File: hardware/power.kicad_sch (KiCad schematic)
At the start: 14 parts, among them U2 LM2596S-ADJ, U3 LM1117-5.0, U4 LM1117-3.3

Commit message: Assign footprints to symbols
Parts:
- C11, C12, C13, C14: footprint (none) -> Capacitor_SMD:C_0603_1608Metric
- D1: value 1N5822 -> SK36A-R2
- F1: footprint (none) -> Fuse:Fuse_1210_3225Metric
- L1: footprint (none) -> Inductor_SMD:L_12x12mm_H6mm
- R4, R5: footprint (none) -> Resistor_SMD:R_0603_1608Metric
- U3, U4: footprint (none) -> Package_TO_SOT_SMD:SOT-223-3_TabPin2
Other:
- moved on the sheet: C9
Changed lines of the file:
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@@
     (stroke (width 0) (type default) (color 0 0 0 0))
   )
-  (wire (pts (xy 85.09 95.25) (xy 85.09 100.33))
+  (wire (pts (xy 85.09 96.52) (xy 85.09 100.33))
     (stroke (width 0) (type default) (color 0 0 0 0))
   )
@@
     (stroke (width 0) (type default) (color 0 0 0 0))
   )
-  (wire (pts (xy 85.09 87.63) (xy 85.09 90.17))
+  (wire (pts (xy 85.09 87.63) (xy 85.09 91.44))
     (stroke (width 0) (type default) (color 0 0 0 0))
   )
@@
       (effects (font (size 1.27 1.27)) (justify left))
     )
-    (property "Footprint" "" (id 2) (at 227.33 97.79 0)
+    (property "Footprint" "Capacitor_SMD:C_0603_1608Metric" (id 2) (at 227.33 97.79 0)
       (effects (font (size 1.27 1.27)) hide)
     )
@@
       (effects (font (size 1.27 1.27)) (justify left))
     )
-    (property "Value" "1N5822" (id 1) (at 115.57 100.0124 90)
+    (property "Value" "SK36A-R2" (id 1) (at 113.03 100.0124 90)
       (effects (font (size 1.27 1.27)) (justify left))
     )
@@
     (property "Reference" "F1" (id 0) (at 76.2 82.55 90))
     (property "Value" "500mA" (id 1) (at 76.2 85.09 90))
-    (property "Footprint" "" (id 2) (at 81.28 86.36 0)
+    (property "Footprint" "Fuse:Fuse_1210_3225Metric" (id 2) (at 81.28 86.36 0)
       (effects (font (size 1.27 1.27)) (justify left) hide)
     )
@@
       (effects (font (size 1.27 1.27)) (justify right))
     )
-    (property "Footprint" "" (id 2) (at 207.01 97.79 0)
+    (property "Footprint" "Capacitor_SMD:C_0603_1608Metric" (id 2) (at 207.01 97.79 0)
       (effects (font (size 1.27 1.27)) hide)
     )
@@
     (property "Reference" "L1" (id 0) (at 130.81 90.17 90))
     (property "Value" "33μH" (id 1) (at 130.81 95.25 90))
-    (property "Footprint" "" (id 2) (at 130.81 92.71 0)
+    (property "Footprint" "Inductor_SMD:L_12x12mm_H6mm" (id 2) (at 130.81 92.71 0)
       (effects (font (size 1.27 1.27)) hide)
     )
@@
       (effects (font (size 1.27 1.27)) (justify left))
     )
-    (property "Footprint" "" (id 2) (at 190.5 97.79 0)
+    (property "Footprint" "Capacitor_SMD:C_0603_1608Metric" (id 2) (at 190.5 97.79 0)
       (effects (font (size 1.27 1.27)) hide)
     )
@@
     (property "Reference" "U4" (id 0) (at 217.17 86.36 0))
     (property "Value" "LM1117-3.3" (id 1) (at 217.17 88.9 0))
-    (property "Footprint" "" (id 2) (at 217.17 92.71 0)
+    (property "Footprint" "Package_TO_SOT_SMD:SOT-223-3_TabPin2" (id 2) (at 217.17 92.71 0)
       (effects (font (size 1.27 1.27)) hide)
     )
@@
     (property "Reference" "U3" (id 0) (at 180.34 86.36 0))
     (property "Value" "LM1117-5.0" (id 1) (at 180.34 88.9 0))
-    (property "Footprint" "" (id 2) (at 180.34 92.71 0)
+    (property "Footprint" "Package_TO_SOT_SMD:SOT-223-3_TabPin2" (id 2) (at 180.34 92.71 0)
       (effects (font (size 1.27 1.27)) hide)
     )
@@
       (effects (font (size 1.27 1.27)) (justify left))
     )
-    (property "Footprint" "" (id 2) (at 152.4 104.14 0)
+    (property "Footprint" "Resistor_SMD:R_0603_1608Metric" (id 2) (at 152.4 104.14 0)
       (effects (font (size 1.27 1.27)) hide)
     )
@@
     (pin "2")
   )
-  (symbol (lib_id "Device:C_Polarized_Small") (at 85.09 92.71 0) (unit 1)
-    (in_bom yes) (on_board yes) (fields_autoplaced)
-    (property "Reference" "C9" (id 0) (at 87.63 90.8938 0)
-      (effects (font (size 1.27 1.27)) (justify left))
-    )
-    (property "Value" "680μF" (id 1) (at 87.63 93.4338 0)
-      (effects (font (size 1.27 1.27)) (justify left))
-    )
-    (property "Footprint" "" (id 2) (at 85.09 92.71 0)
-      (effects (font (size 1.27 1.27)) hide)
-    )
-    (property "Datasheet" "~" (id 3) (at 85.09 92.71 0)
+  (symbol (lib_id "Device:C_Polarized_Small") (at 85.09 93.98 0) (unit 1)
+    (in_bom yes) (on_board yes) (fields_autoplaced)
+    (property "Reference" "C9" (id 0) (at 87.63 92.1638 0)
+      (effects (font (size 1.27 1.27)) (justify left))
+    )
+    (property "Value" "680μF" (id 1) (at 87.63 94.7038 0)
+      (effects (font (size 1.27 1.27)) (justify left))
+    )
+    (property "Footprint" "" (id 2) (at 85.09 93.98 0)
+      (effects (font (size 1.27 1.27)) hide)
+    )
+    (property "Datasheet" "~" (id 3) (at 85.09 93.98 0)
       (effects (font (size 1.27 1.27)) hide)
     )
@@
       (effects (font (size 1.27 1.27)) (justify right))
     )
-    (property "Footprint" "" (id 2) (at 170.18 97.79 0)
+    (property "Footprint" "Capacitor_SMD:C_0603_1608Metric" (id 2) (at 170.18 97.79 0)
       (effects (font (size 1.27 1.27)) hide)
     )
@@
       (effects (font (size 1.27 1.27)) (justify left))
     )
-    (property "Footprint" "" (id 2) (at 152.4 96.52 0)
-      (effects (font (size 1.27 1.27)) hide)
-    )
+    (property "Footprint" "Resistor_SMD:R_0603_1608Metric" (id 2) (at 152.4 96.52 0)
+      (effects (font (size 1.27 1.27)) hide)
+    )

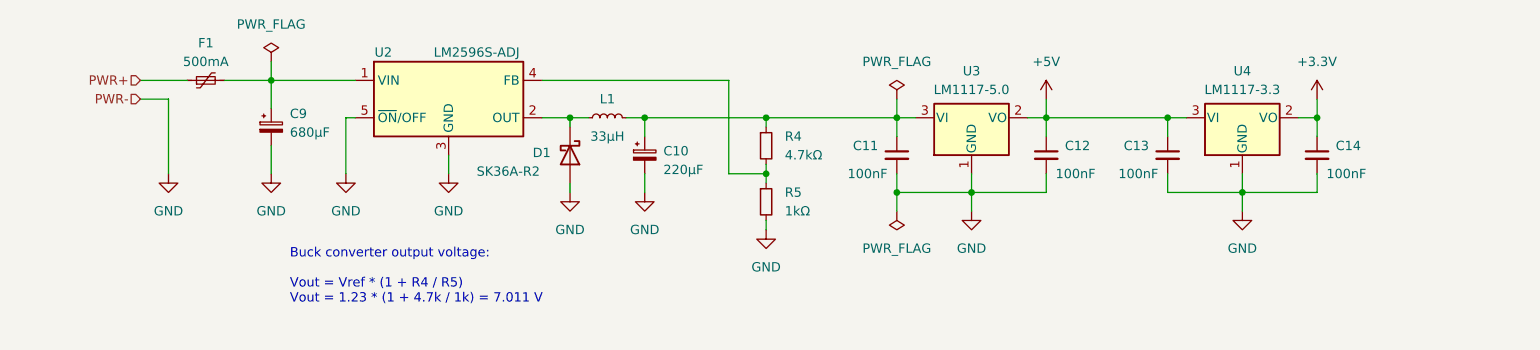
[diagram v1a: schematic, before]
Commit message: Use more efficient buck converter
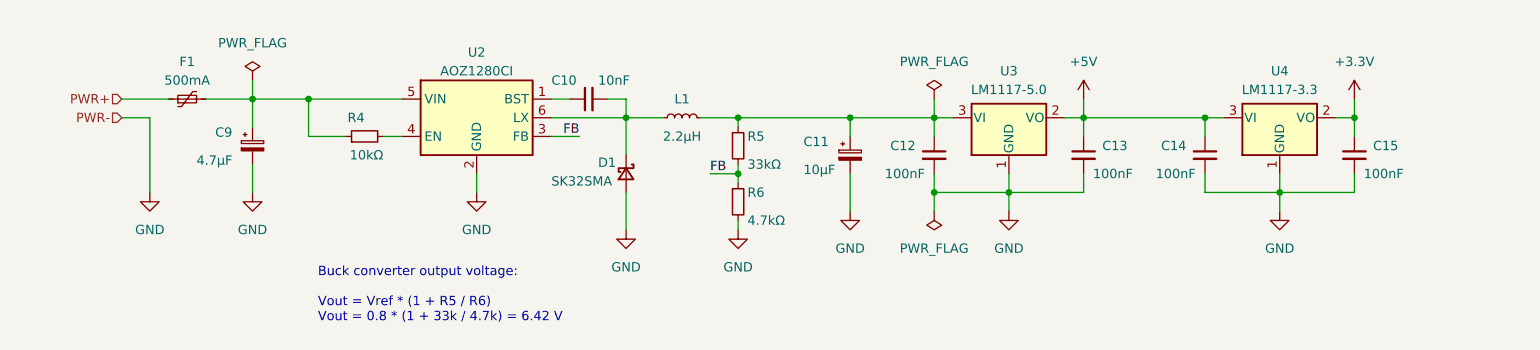
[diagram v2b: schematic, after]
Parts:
- removed D1: SK36A-R2, Diode_THT:D_DO-201AD_P15.24mm_Horizontal, symbol Diode:1N5822
- removed U2: LM2596S-ADJ, Package_TO_SOT_SMD:TO-263-5_TabPin3, symbol Regulator_Switching:LM2596S-ADJ
- added C10: 10nF, Capacitor_SMD:C_0603_1608Metric, symbol Device:C_Small
- added D1: SK32SMA, Diode_SMD:D_SMA, symbol Device:D_Schottky_Small
- added R4: 10kΩ, Resistor_SMD:R_0603_1608Metric, symbol Device:R_Small
- added U2: AOZ1280CI, Package_TO_SOT_SMD:SOT-23-6, symbol Regulator_Switching:AOZ1280CI
- C11: renamed from C10; value 220μF -> 10μF; footprint (none) -> Capacitor_SMD:C_Elec_4x5.4
- C9: value 680μF -> 4.7μF; footprint (none) -> Capacitor_SMD:C_Elec_4x5.4
- L1: value 33μH -> 2.2μH; footprint Inductor_SMD:L_12x12mm_H6mm -> Inductor_SMD:L_Bourns-SRN4018
- R5: renamed from R4; value 4.7kΩ -> 33kΩ
- R6: renamed from R5; value 1kΩ -> 4.7kΩ
- renumbered C11 to C12, C12 to C13, C13 to C14, C14 to C15
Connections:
- net GND: now also D1.2 (A), U2.2 (GND)
- net at C9.1, F1.2: now also R4.1, U2.5 (VIN)
- net at L1.1: now also C10.2, D1.1 (K), U2.6 (LX)
- net FB: now reaches R5.2, R6.1
- net FB: now also U2.3 (FB)
- new net: C10.1, U2.1 (BST)
- new net: R4.2, U2.4 (EN)
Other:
- note added: "Buck converter output voltage: Vout = Vref * (1 + R5 / R6) Vout = 0.8 * (1 + 33k / 4.7k) = 6.42 V"
- note removed: "Buck converter output voltage: Vout = Vref * (1 + R4 / R5) Vout = 1.23 * (1 + 4.7k / 1k) = 7.011 V"
- moved on the sheet: C11, C12, C13, C14, C15, C9, F1, L1, R5, R6, U3, U4

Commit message: Arrange footprints
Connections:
- net 6.42V: now reaches C11.1, C12.1, L1.2, R5.1, U3.3 (VI)
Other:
- title: Power Delivery -> Power Supply
- moved on the sheet: C11
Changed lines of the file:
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@@
   (paper "A4")
   (title_block
-    (title "Power Delivery")
-    (date "2022-12-04")
-    (rev "0.1.0")
+    (title "Power Supply")
+    (date "2022-12-10")
+    (rev "${REVISION}")
     (company "PUT Motorsport")
-    (comment 1 "Author: I. Kajdan")
+    (comment 3 "Reviewer:")
+    (comment 4 "Author: I. Kajdan")
   )
   (junction (at 175.26 102.87) (diameter 0) (color 0 0 0 0)
@@
   (junction (at 195.58 92.71) (diameter 0) (color 0 0 0 0)
   )
-  (junction (at 163.83 92.71) (diameter 0) (color 0 0 0 0)
+  (junction (at 162.56 92.71) (diameter 0) (color 0 0 0 0)
   )
   (junction (at 175.26 92.71) (diameter 0) (color 0 0 0 0)
@@
     (stroke (width 0) (type default) (color 0 0 0 0))
   )
-  (wire (pts (xy 163.83 92.71) (xy 163.83 95.25))
+  (wire (pts (xy 162.56 92.71) (xy 162.56 95.25))
     (stroke (width 0) (type default) (color 0 0 0 0))
   )
@@
     (stroke (width 0) (type default) (color 0 0 0 0))
   )
-  (wire (pts (xy 163.83 92.71) (xy 175.26 92.71))
+  (wire (pts (xy 162.56 92.71) (xy 175.26 92.71))
     (stroke (width 0) (type default) (color 0 0 0 0))
   )
@@
     (stroke (width 0) (type default) (color 0 0 0 0))
   )
-  (wire (pts (xy 163.83 100.33) (xy 163.83 105.41))
+  (wire (pts (xy 162.56 100.33) (xy 162.56 105.41))
     (stroke (width 0) (type default) (color 0 0 0 0))
   )
@@
     (stroke (width 0) (type default) (color 0 0 0 0))
   )
+  (wire (pts (xy 148.59 92.71) (xy 162.56 92.71))
+    (stroke (width 0) (type default) (color 0 0 0 0))
+  )
   (wire (pts (xy 90.17 90.17) (xy 102.87 90.17))
     (stroke (width 0) (type default) (color 0 0 0 0))
@@
   )
   (wire (pts (xy 82.55 99.06) (xy 82.55 102.87))
-    (stroke (width 0) (type default) (color 0 0 0 0))
-  )
-  (wire (pts (xy 148.59 92.71) (xy 163.83 92.71))
     (stroke (width 0) (type default) (color 0 0 0 0))
   )
@@
     (effects (font (size 1.27 1.27)) (justify left bottom))
   )
+  (label "6.42V" (at 156.21 92.71 0)
+    (effects (font (size 1.27 1.27)) (justify left bottom))
+  )
   (label "FB" (at 144.78 100.33 0)
     (effects (font (size 1.27 1.27)) (justify left bottom))
@@
     (pin "1")
   )
-  (symbol (lib_id "power:GND") (at 163.83 105.41 0) (unit 1)
-    (in_bom yes) (on_board yes) (fields_autoplaced)
-    (property "Reference" "#PWR018" (id 0) (at 163.83 111.76 0)
-      (effects (font (size 1.27 1.27)) hide)
-    )
-    (property "Value" "GND" (id 1) (at 163.83 110.49 0))
-    (property "Footprint" "" (id 2) (at 163.83 105.41 0)
-      (effects (font (size 1.27 1.27)) hide)
-    )
-    (property "Datasheet" "" (id 3) (at 163.83 105.41 0)
+  (symbol (lib_id "power:GND") (at 162.56 105.41 0) (unit 1)
+    (in_bom yes) (on_board yes) (fields_autoplaced)
+    (property "Reference" "#PWR018" (id 0) (at 162.56 111.76 0)
+      (effects (font (size 1.27 1.27)) hide)
+    )
+    (property "Value" "GND" (id 1) (at 162.56 110.49 0))
+    (property "Footprint" "" (id 2) (at 162.56 105.41 0)
+      (effects (font (size 1.27 1.27)) hide)
+    )
+    (property "Datasheet" "" (id 3) (at 162.56 105.41 0)
       (effects (font (size 1.27 1.27)) hide)
     )
@@
     (pin "2")
   )
-  (symbol (lib_id "Device:C_Polarized_Small") (at 163.83 97.79 0) (unit 1)
-    (in_bom yes) (on_board yes)
-    (property "Reference" "C11" (id 0) (at 157.48 95.9738 0)
-      (effects (font (size 1.27 1.27)) (justify left))
-    )
-    (property "Value" "10μF" (id 1) (at 157.48 99.7838 0)
-      (effects (font (size 1.27 1.27)) (justify left))
-    )
-    (property "Footprint" "Capacitor_SMD:C_Elec_4x5.4" (id 2) (at 163.83 97.79 0)
-      (effects (font (size 1.27 1.27)) hide)
-    )
-    (property "Datasheet" "~" (id 3) (at 163.83 97.79 0)
+  (symbol (lib_id "Device:C_Polarized_Small") (at 162.56 97.79 0) (unit 1)
+    (in_bom yes) (on_board yes)
+    (property "Reference" "C11" (id 0) (at 156.21 95.9738 0)
+      (effects (font (size 1.27 1.27)) (justify left))
+    )
+    (property "Value" "10μF" (id 1) (at 156.21 101.0538 0)
+      (effects (font (size 1.27 1.27)) (justify left))
+    )
+    (property "Footprint" "Capacitor_SMD:C_Elec_4x5.4" (id 2) (at 162.56 97.79 0)
+      (effects (font (size 1.27 1.27)) hide)
+    )
+    (property "Datasheet" "~" (id 3) (at 162.56 97.79 0)
       (effects (font (size 1.27 1.27)) hide)
     )
@@
       (effects (font (size 1.27 1.27)) (justify left))
     )
-    (property "Value" "4.7μF" (id 1) (at 74.93 98.5138 0)
-      (effects (font (size 1.27 1.27)) (justify left))
-    )
+    (property "Value" "4.7μF" (id 1) (at 74.93 99.7838 0)
+      (effects (font (size 1.27 1.27)) (justify left))
+    )

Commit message: Apply PUTM branding
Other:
- company: PUT Motorsport -> Author: I. Kajdan
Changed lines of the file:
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@@
   (title_block
     (title "Power Supply")
-    (date "2022-12-10")
+    (date "2022-12-11")
     (rev "${REVISION}")
-    (company "PUT Motorsport")
-    (comment 3 "Reviewer:")
-    (comment 4 "Author: I. Kajdan")
+    (company "Author: I. Kajdan")
   )
   (junction (at 175.26 102.87) (diameter 0) (color 0 0 0 0)

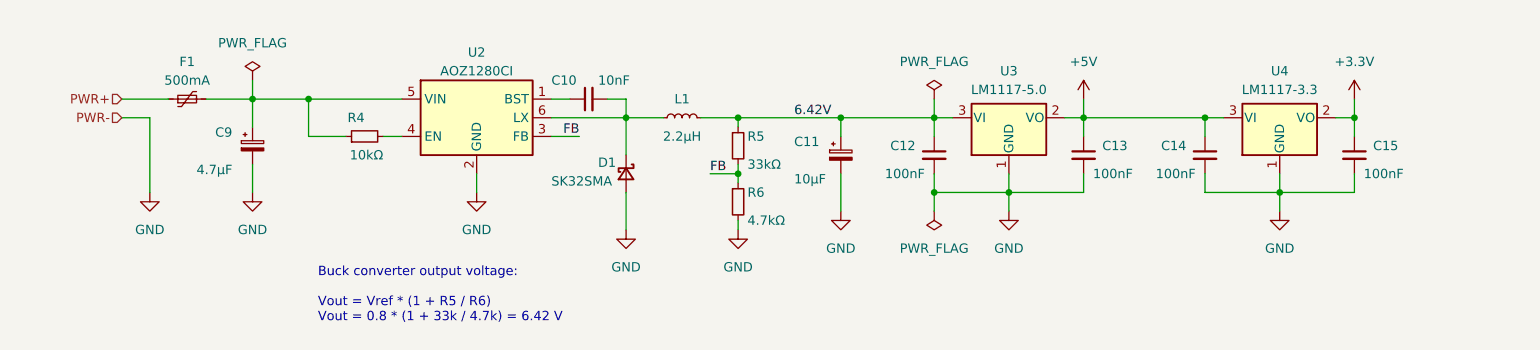
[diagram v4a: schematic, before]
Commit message: Miscellaneous changes
- Use THT connectors
- Adjust ADC circuit according to the datasheet
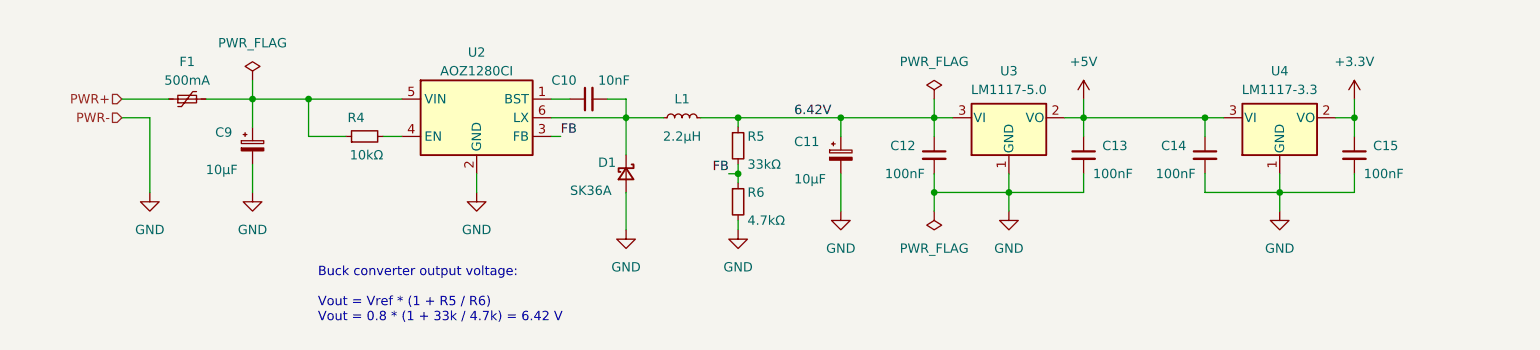
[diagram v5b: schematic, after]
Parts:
- C11: footprint Capacitor_SMD:C_Elec_4x5.4 -> Capacitor_SMD:CP_Elec_6.3x5.4
- C9: value 4.7μF -> 10μF; footprint Capacitor_SMD:C_Elec_4x5.4 -> Capacitor_SMD:CP_Elec_6.3x5.4
- D1: value SK32SMA -> SK36A
- F1: footprint Fuse:Fuse_1210_3225Metric -> Fuse:Fuse_0805_2012Metric
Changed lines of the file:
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@@
     (stroke (width 0) (type default) (color 0 0 0 0))
   )
-  (wire (pts (xy 144.78 100.33) (xy 148.59 100.33))
+  (wire (pts (xy 147.32 100.33) (xy 148.59 100.33))
     (stroke (width 0) (type default) (color 0 0 0 0))
   )
@@
     (stroke (width 0) (type default) (color 0 0 0 0))
   )
-  (wire (pts (xy 123.19 95.25) (xy 127 95.25))
+  (wire (pts (xy 123.19 95.25) (xy 124.46 95.25))
     (stroke (width 0) (type default) (color 0 0 0 0))
   )
@@
     (effects (font (size 1.27 1.27)) (justify left bottom))
   )
-  (label "FB" (at 144.78 100.33 0)
+  (label "FB" (at 147.32 100.33 180)
+    (effects (font (size 1.27 1.27)) (justify right bottom))
+  )
+  (label "FB" (at 124.46 95.25 0)
     (effects (font (size 1.27 1.27)) (justify left bottom))
-  )
-  (label "FB" (at 127 95.25 180)
-    (effects (font (size 1.27 1.27)) (justify right bottom))
   )
   (hierarchical_label "PWR+" (shape input) (at 64.77 90.17 180)
@@
     (property "Reference" "F1" (id 0) (at 73.66 85.09 90))
     (property "Value" "500mA" (id 1) (at 73.66 87.63 90))
-    (property "Footprint" "Fuse:Fuse_1210_3225Metric" (id 2) (at 78.74 88.9 0)
+    (property "Footprint" "Fuse:Fuse_0805_2012Metric" (id 2) (at 78.74 88.9 0)
       (effects (font (size 1.27 1.27)) (justify left) hide)
     )
@@
       (effects (font (size 1.27 1.27)) (justify left))
     )
-    (property "Value" "SK32SMA" (id 1) (at 123.19 101.3459 90)
+    (property "Value" "SK36A" (id 1) (at 125.73 102.6159 90)
       (effects (font (size 1.27 1.27)) (justify left))
     )
@@
       (effects (font (size 1.27 1.27)) (justify left))
     )
-    (property "Footprint" "Capacitor_SMD:C_Elec_4x5.4" (id 2) (at 162.56 97.79 0)
+    (property "Footprint" "Capacitor_SMD:CP_Elec_6.3x5.4" (id 2) (at 162.56 97.79 0)
       (effects (font (size 1.27 1.27)) hide)
     )
@@
       (effects (font (size 1.27 1.27)) (justify left))
     )
-    (property "Value" "4.7μF" (id 1) (at 74.93 99.7838 0)
-      (effects (font (size 1.27 1.27)) (justify left))
-    )
-    (property "Footprint" "Capacitor_SMD:C_Elec_4x5.4" (id 2) (at 82.55 96.52 0)
-      (effects (font (size 1.27 1.27)) hide)
-    )
+    (property "Value" "10μF" (id 1) (at 76.2 99.7838 0)
+      (effects (font (size 1.27 1.27)) (justify left))
+    )
+    (property "Footprint" "Capacitor_SMD:CP_Elec_6.3x5.4" (id 2) (at 82.55 96.52 0)
+      (effects (font (size 1.27 1.27)) hide)
+    )

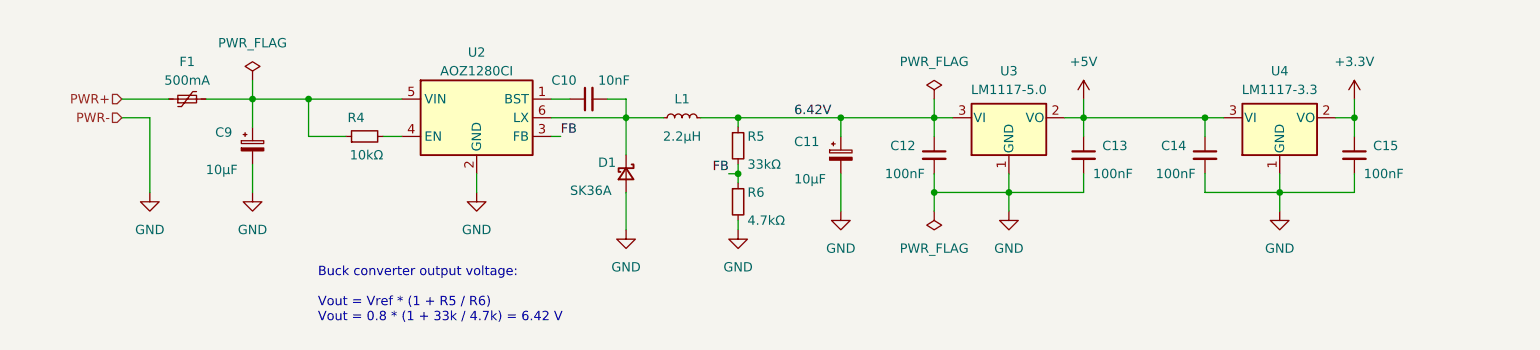
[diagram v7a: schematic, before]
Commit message: Improve routing around the buck converter
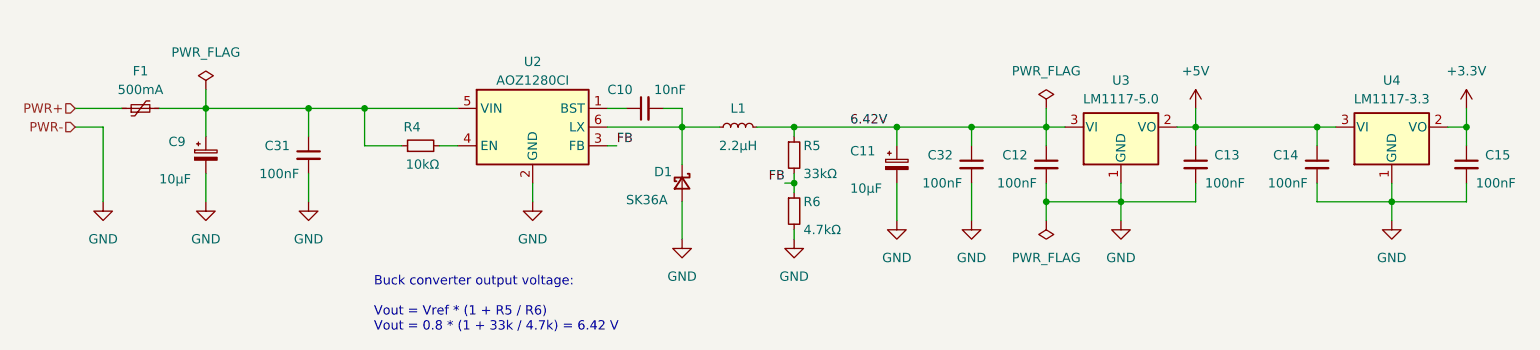
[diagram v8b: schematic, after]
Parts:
- added C31, C32: 100nF, Capacitor_SMD:C_0603_1608Metric, symbol Device:C_Small
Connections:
- net 6.42V: now also C32.1
- net GND: now also C31.2, C32.2
- net at C9.1, F1.2, R4.1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: now also C31.1
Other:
- moved on the sheet: C10, C11, C12, C13, C14, C15, C9, D1, F1, L1, R4, R5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
